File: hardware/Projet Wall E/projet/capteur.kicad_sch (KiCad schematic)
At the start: 0 parts

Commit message: feat: ajout du schéma des capteurs
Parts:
- added C25, C27, C29: 100nF, Capacitor_SMD:C_0603_1608Metric, symbol wall_e:C
- added C26, C28, C30: 10uF, Capacitor_SMD:C_0603_1608Metric, symbol wall_e:C
- added J6, J7, J8: Conn_01x06, Connector_JST:JST_PH_B6B-PH-K_1x06_P2.00mm_Vertical, symbol Connector_Generic:Conn_01x06
- added R18, R19: 4.7k, Resistor_SMD:R_0603_1608Metric, symbol wall_e:R
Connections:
- new net: C29.1, C30.1, J8.1 (Pin_1)
- new net +3.3V: C25.1, C26.1, C27.1, C28.1, J6.1 (Pin_1), J7.1 (Pin_1), J8.2 (Pin_2), R18.1, R19.1
- new net APDS_INT: J8.6 (Pin_6)
- new net GND: C25.2, C26.2, C27.2, C28.2, C29.2, C30.2, J6.2 (Pin_2), J7.2 (Pin_2), J8.3 (Pin_3)
- new net SCL_CAPT: J6.3 (Pin_3), J7.3 (Pin_3), J8.4 (Pin_4), R18.2
- new net SDA_CAPT: J6.4 (Pin_4), J7.4 (Pin_4), J8.5 (Pin_5), R19.2
- new net TOF_L_GPIO1: J6.5 (Pin_5)
- new net TOF_L_XSHUT: J6.6 (Pin_6)
- new net TOF_R_GPIO1: J7.5 (Pin_5)
- new net TOF_R_XSHUT: J7.6 (Pin_6)
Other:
- note added: "COULEUR"
- note added: "PULL-UPS I2C"
- note added: "ToF DROIT"
- note added: "ToF GAUCHE"

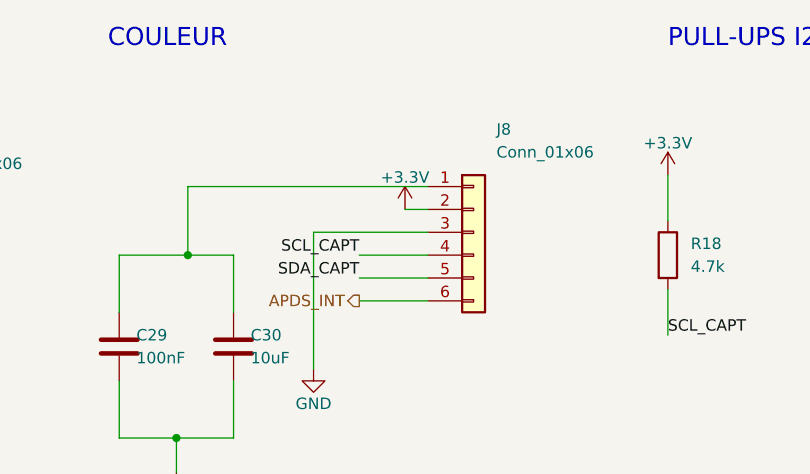
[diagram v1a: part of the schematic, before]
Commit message: feat: mise à jour du schéma capteurs
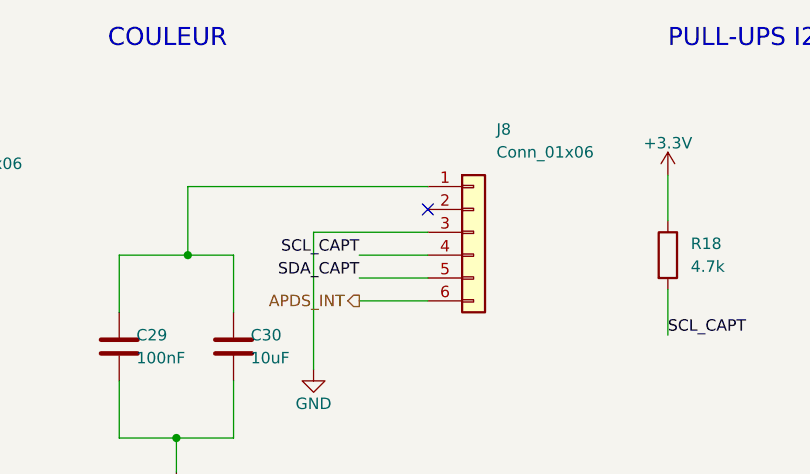
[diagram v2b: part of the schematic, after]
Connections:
- net +3.3V: no longer J8.2 (Pin_2)
- no-connect marks 0 -> 1
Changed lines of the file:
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@@
 		(color 0 0 0 0)
 	)
+	(no_connect
+		(at 214.63 85.09)
+	)
 	(wire
 		(pts
@@
 		(pts
 			(xy 30.48 104.14) (xy 30.48 110.49)
-		)
-		(stroke
-			(width 0)
-			(type default)
-		)
-	)
-	(wire
-		(pts
-			(xy 212.09 85.09) (xy 214.63 85.09)
 		)
 		(stroke
@@
 					(unit 1)
 				)
-			)
-		)
-	)
-	(symbol
-		(lib_id "power:+3.3V")
-		(at 212.09 85.09 0)
-		(unit 1)
-		(body_style 1)
-		(exclude_from_sim no)
-		(in_bom yes)
-		(on_board yes)
-		(in_pos_files yes)
-		(dnp no)
-		(property "Reference" "#PWR053"
-			(at 212.09 88.646 0)
-			(hide yes)
-			(show_name no)
-			(do_not_autoplace no)
-			(effects
-				(font
-					(size 1.27 1.27)
-				)
-			)
-		)
-		(property "Value" "+3.3V"
-			(at 212.09 81.534 0)
-			(show_name no)
-			(do_not_autoplace no)
-			(effects
-				(font
-					(size 1.27 1.27)
-				)
-			)
-		)
-		(property "Footprint" ""
-			(at 212.09 85.09 0)
-			(hide yes)
-			(show_name no)
-			(do_not_autoplace no)
-			(effects
-				(font
-					(size 1.27 1.27)
-				)
-			)
-		)
-		(property "Datasheet" ""
-			(at 212.09 85.09 0)
-			(show_name no)
-			(do_not_autoplace no)
-			(effects
-				(font
-					(size 1.27 1.27)
-				)
-			)
-		)
-		(property "Description" ""
-			(at 212.09 85.09 0)
-			(show_name no)
-			(do_not_autoplace no)
-			(effects
-				(font
-					(size 1.27 1.27)
-				)
-			)
-		)
-		(pin "1"
-		)
-		(instances
-			(project "projet"
-				(path "/aad9219d-d686-4d68-8dbb-b3c2b0727159/23293480-63ec-471b-bf54-55169cccd8a3"
-					(reference "#PWR053")
-					(unit 1)
-				)

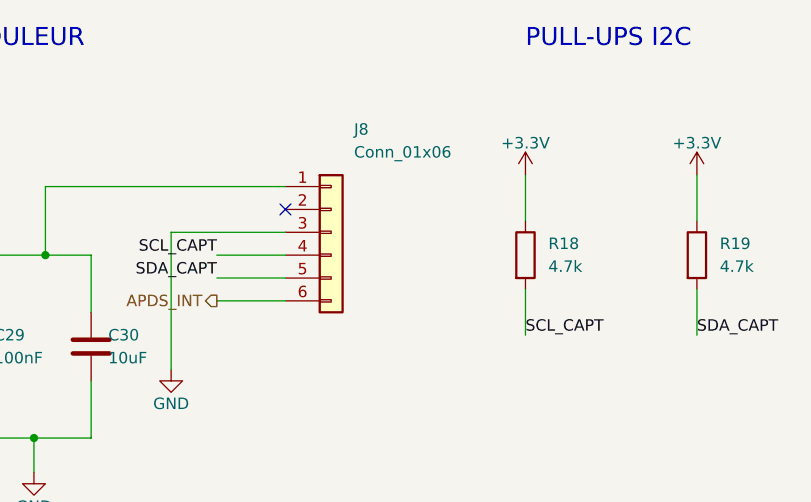
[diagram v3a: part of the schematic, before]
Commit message: feat: mise a jour capteur et projet: empreintes
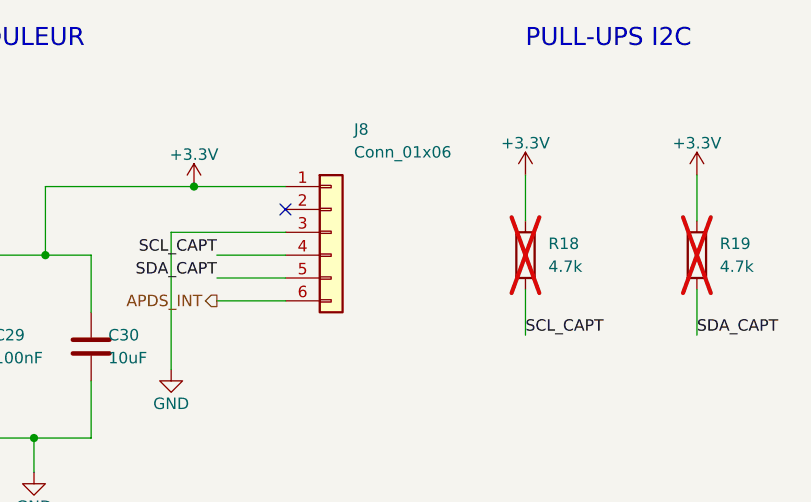
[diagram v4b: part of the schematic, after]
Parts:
- C25: footprint Capacitor_SMD:C_0603_1608Metric -> Capacitor_SMD:C_0603_1608Metric_Pad1.08x0.95mm_HandSolder
- C26, C27, C28, C29, C30: footprint Capacitor_SMD:C_0603_1608Metric -> Capacitor_SMD:C_0402_1005Metric
- J6, J7, J8: footprint Connector_JST:JST_PH_B6B-PH-K_1x06_P2.00mm_Vertical -> Connector_PinHeader_2.54mm:PinHeader_1x06_P2.54mm_Vertical
- R18, R19: footprint Resistor_SMD:R_0603_1608Metric -> Resistor_SMD:R_0402_1005Metric; now not fitted
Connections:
- net +3.3V: now also C29.1, C30.1, J8.1 (Pin_1)
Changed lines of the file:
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@@
+	)
+	(junction
+		(at 204.47 82.55)
+		(diameter 0)
+		(color 0 0 0 0)
 	)
 	(junction
@@
 			)
 		)
-		(property "Footprint" "Capacitor_SMD:C_0603_1608Metric"
+		(property "Footprint" "Capacitor_SMD:C_0402_1005Metric"
 			(at 43.18 100.33 0)
 			(hide yes)
@@
 				(path "/aad9219d-d686-4d68-8dbb-b3c2b0727159/23293480-63ec-471b-bf54-55169cccd8a3"
 					(reference "C26")
+					(unit 1)
+				)
+			)
+		)
+	)
+	(symbol
+		(lib_id "power:+3.3V")
+		(at 204.47 82.55 0)
+		(unit 1)
+		(body_style 1)
+		(exclude_from_sim no)
+		(in_bom yes)
+		(on_board yes)
+		(in_pos_files yes)
+		(dnp no)
+		(property "Reference" "#PWR056"
+			(at 204.47 86.106 0)
+			(hide yes)
+			(show_name no)
+			(do_not_autoplace no)
+			(effects
+				(font
+					(size 1.27 1.27)
+				)
+			)
+		)
+		(property "Value" "+3.3V"
+			(at 204.47 78.994 0)
+			(show_name no)
+			(do_not_autoplace no)
+			(effects
+				(font
+					(size 1.27 1.27)
+				)
+			)
+		)
+		(property "Footprint" ""
+			(at 204.47 82.55 0)
+			(hide yes)
+			(show_name no)
+			(do_not_autoplace no)
+			(effects
+				(font
+					(size 1.27 1.27)
+				)
+			)
+		)
+		(property "Datasheet" ""
+			(at 204.47 82.55 0)
+			(show_name no)
+			(do_not_autoplace no)
+			(effects
+				(font
+					(size 1.27 1.27)
+				)
+			)
+		)
+		(property "Description" ""
+			(at 204.47 82.55 0)
+			(show_name no)
+			(do_not_autoplace no)
+			(effects
+				(font
+					(size 1.27 1.27)
+				)
+			)
+		)
+		(pin "1"
+		)
+		(instances
+			(project "projet"
+				(path "/aad9219d-d686-4d68-8dbb-b3c2b0727159/23293480-63ec-471b-bf54-55169cccd8a3"
+					(reference "#PWR056")
 					(unit 1)
 				)
@@
 			)
 		)
-		(property "Footprint" "Capacitor_SMD:C_0603_1608Metric"
+		(property "Footprint" "Capacitor_SMD:C_0402_1005Metric"
 			(at 106.68 97.79 0)
 			(hide yes)
@@
 			)
 		)
-		(property "Footprint" "Connector_JST:JST_PH_B6B-PH-K_1x06_P2.00mm_Vertical"
+		(property "Footprint" "Connector_PinHeader_2.54mm:PinHeader_1x06_P2.54mm_Vertical"
 			(at 219.71 87.63 0)
 			(hide yes)
@@
 			)
 		)
-		(property "Footprint" "Capacitor_SMD:C_0603_1608Metric"
+		(property "Footprint" "Capacitor_SMD:C_0603_1608Metric_Pad1.08x0.95mm_HandSolder"
 			(at 30.48 100.33 0)
 			(hide yes)
@@
 			)
 		)
-		(property "Footprint" "Capacitor_SMD:C_0603_1608Metric"
+		(property "Footprint" "Capacitor_SMD:C_0402_1005Metric"
 			(at 119.38 97.79 0)
 			(hide yes)
@@
 		(on_board yes)
 		(in_pos_files yes)
-		(dnp no)
+		(dnp yes)
 		(property "Reference" "R18"
 			(at 243.84 88.9 0)
@@
 			)
 		)
-		(property "Footprint" "Resistor_SMD:R_0603_1608Metric"
+		(property "Footprint" "Resistor_SMD:R_0402_1005Metric"
 			(at 241.3 90.17 0)
 			(hide yes)
@@
 			)
 		)
-		(property "Footprint" "Capacitor_SMD:C_0603_1608Metric"
+		(property "Footprint" "Capacitor_SMD:C_0402_1005Metric"
 			(at 180.34 100.33 0)
 			(hide yes)
@@
 			)
 		)
-		(property "Footprint" "Capacitor_SMD:C_0603_1608Metric"
+		(property "Footprint" "Capacitor_SMD:C_0402_1005Metric"
 			(at 193.04 100.33 0)
 			(hide yes)
@@
 			)
 		)
-		(property "Footprint" "Connector_JST:JST_PH_B6B-PH-K_1x06_P2.00mm_Vertical"
+		(property "Footprint" "Connector_PinHeader_2.54mm:PinHeader_1x06_P2.54mm_Vertical"
 			(at 76.2 90.17 0)
 			(hide yes)
@@
 			)
 		)
-		(property "Footprint" "Connector_JST:JST_PH_B6B-PH-K_1x06_P2.00mm_Vertical"
+		(property "Footprint" "Connector_PinHeader_2.54mm:PinHeader_1x06_P2.54mm_Vertical"
 			(at 156.21 88.9 0)
 			(hide yes)
@@
 		(on_board yes)
 		(in_pos_files yes)
-		(dnp no)
+		(dnp yes)
 		(property "Reference" "R19"
 			(at 262.89 88.9 0)
@@
 			)
 		)
-		(property "Footprint" "Resistor_SMD:R_0603_1608Metric"
+		(property "Footprint" "Resistor_SMD:R_0402_1005Metric"
 			(at 260.35 90.17 0)
 			(hide yes)
@@
 		)
 	)
-	(embedded_fonts no)
 )

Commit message: feat: mise a jour alim reference jlcpcb
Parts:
- C25, C27, C29: JLCPCB Part # (none) -> C1525
- C26, C28, C30: JLCPCB Part # (none) -> C15525
- R18, R19: JLCPCB Part # (none) -> C850286
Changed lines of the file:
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@@
+			)
+		)
+		(property "JLCPCB Part #" "C15525"
+			(at 43.18 100.33 0)
+			(hide yes)
+			(show_name no)
+			(do_not_autoplace no)
+			(effects
+				(font
+					(size 1.27 1.27)
+				)
 			)
 		)
@@
 			)
 		)
+		(property "JLCPCB Part #" "C1525"
+			(at 106.68 97.79 0)
+			(hide yes)
+			(show_name no)
+			(do_not_autoplace no)
+			(effects
+				(font
+					(size 1.27 1.27)
+				)
+			)
+		)
 		(pin "1"
 		)
@@
 			)
 		)
+		(property "JLCPCB Part #" "C1525"
+			(at 30.48 100.33 0)
+			(hide yes)
+			(show_name no)
+			(do_not_autoplace no)
+			(effects
+				(font
+					(size 1.27 1.27)
+				)
+			)
+		)
 		(pin "1"
 		)
@@
 		(property "Description" ""
 			(at 119.38 97.79 0)
+			(show_name no)
+			(do_not_autoplace no)
+			(effects
+				(font
+					(size 1.27 1.27)
+				)
+			)
+		)
+		(property "JLCPCB Part #" "C15525"
+			(at 119.38 97.79 0)
+			(hide yes)
 			(show_name no)
 			(do_not_autoplace no)
@@
 			)
 		)
+		(property "JLCPCB Part #" "C850286"
+			(at 241.3 90.17 0)
+			(hide yes)
+			(show_name no)
+			(do_not_autoplace no)
+			(effects
+				(font
+					(size 1.27 1.27)
+				)
+			)
+		)
 		(pin "1"
 		)
@@
 			)
 		)
+		(property "JLCPCB Part #" "C1525"
+			(at 180.34 100.33 0)
+			(hide yes)
+			(show_name no)
+			(do_not_autoplace no)
+			(effects
+				(font
+					(size 1.27 1.27)
+				)
+			)
+		)
 		(pin "1"
 		)
@@
 		(property "Description" ""
 			(at 193.04 100.33 0)
+			(show_name no)
+			(do_not_autoplace no)
+			(effects
+				(font
+					(size 1.27 1.27)
+				)
+			)
+		)
+		(property "JLCPCB Part #" "C15525"
+			(at 193.04 100.33 0)
+			(hide yes)
 			(show_name no)
 			(do_not_autoplace no)
@@
 			(show_name no)
 			(do_not_autoplace no)
+			(effects
+				(font
+					(size 1.27 1.27)
+				)
+			)
+		)
+		(property "JLCPCB Part #" "C850286"
+			(at 260.35 90.17 0)
+			(hide yes)
+			(show_name no)
+			(do_not_autoplace no)

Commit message: Intégration feuille capteurs depuis feature-capteurs
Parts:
- C25: footprint Capacitor_SMD:C_0603_1608Metric_Pad1.08x0.95mm_HandSolder -> Capacitor_SMD:C_0402_1005Metric; JLCPCB Part (none) -> C1525; JLCPCB Part # C1525 -> (none)
- C26, C28, C30: JLCPCB Part (none) -> C15525; JLCPCB Part # C15525 -> (none)
- C27, C29: JLCPCB Part (none) -> C1525; JLCPCB Part # C1525 -> (none)
- R18, R19: JLCPCB Part (none) -> C850286; JLCPCB Part # C850286 -> (none)

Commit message: ajout neopixel
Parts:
- added C507, C508, C509: 100n, Capacitor_SMD:C_0402_1005Metric, symbol Device:C_Small
- added D5: WS2812B, LED_SMD:LED_WS2812B-Mini_PLCC4_3.5x3.5mm, symbol LED:WS2812B
- added J1: Conn_01x03, Connector_Audio:Jack_XLR_Neutrik_NC3FAAH_Horizontal, symbol Connector_Generic:Conn_01x03
- added U6: SN74AHCT1G125DBVR, Package_TO_SOT_SMD:SOT-23-5, symbol 74xGxx:74AHCT1G125
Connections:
- net GND: now also C507.2, C508.1, C509.2, D5.3 (VSS), J1.3 (Pin_3), U6.1, U6.3 (GND)
- new net NEOPIXEL: U6.2
- new net NP_5V: D5.4 (DIN), J1.2 (Pin_2), U6.4
- new net VBUS: C507.1, C508.2, C509.1, D5.1 (VDD), J1.1 (Pin_1), U6.5 (VCC)
- no-connect marks 1 -> 2
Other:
- note added: "NEOPIXEL RGB LED"
